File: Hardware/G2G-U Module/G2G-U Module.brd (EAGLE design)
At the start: 13.1 x 12.8 mm, 4 parts, among them J1 GROVE-4P-2.0-3470130P1

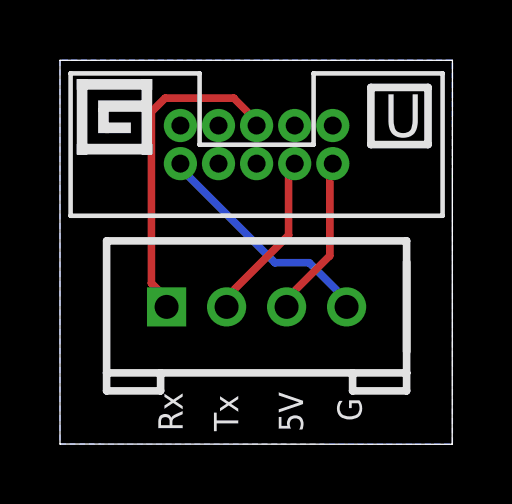
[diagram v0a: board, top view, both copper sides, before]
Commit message: Rotated the G plug 180 degrees.
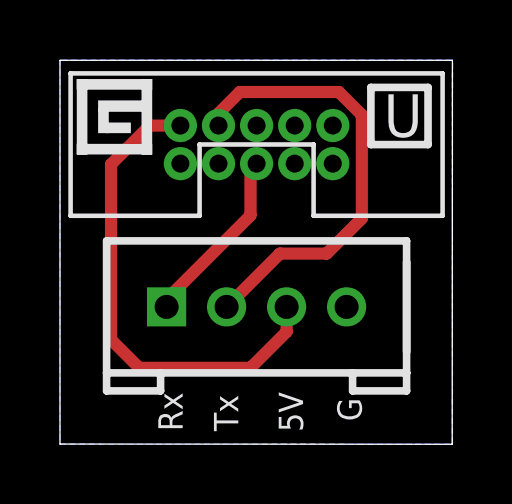
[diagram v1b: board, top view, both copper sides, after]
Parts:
- turned U$1 to 180 degrees
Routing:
- net +5V: track 5.39 -> 16.3 mm
- net TX: track 5.75 -> 15.0 mm
- net GND: track 7.74 -> 0.00 mm
- net RX: track 10.9 -> 6.02 mm
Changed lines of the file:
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@@
 <element name="J1" library="SoftDust" package="4P-2.0" value="GROVE-4P-2.0-3470130P1" x="6.5532" y="4.572" smashed="yes"/>
 <element name="LOGO1" library="SparkFun-Aesthetics" package="OSHW-LOGO-S" value="OSHW-LOGOS" x="1.8796" y="1.778" rot="MR0"/>
-<element name="U$1" library="SoftDust" package="2X5_1.27MM_FEMALE_PLUG" value="2X5_1.27MM_FEMALE_PLUG" x="6.5532" y="9.9822" rot="MR0"/>
+<element name="U$1" library="SoftDust" package="2X5_1.27MM_FEMALE_PLUG" value="2X5_1.27MM_FEMALE_PLUG" x="6.5532" y="9.9822" rot="MR180"/>
 <element name="FRAME1" library="SparkFun-Aesthetics" package="DUMMY" value="" x="0" y="-1.27">
 <attribute name="VERSION" value="v1.0" x="0" y="-1.27" size="1.778" layer="27" display="off"/>
@@
 <contactref element="U$1" pad="4"/>
 <contactref element="J1" pad="2"/>
-<wire x1="7.62" y1="6.9596" x2="7.62" y2="9.2456" width="0.254" layer="1"/>
-<wire x1="5.5626" y1="4.9022" x2="7.62" y2="6.9596" width="0.254" layer="1"/>
-<wire x1="7.62" y1="9.2456" x2="7.8232" y2="9.3472" width="0.254" layer="1"/>
-<wire x1="5.5626" y1="4.9022" x2="5.5532" y2="4.572" width="0.254" layer="1"/>
+<wire x1="5.5532" y1="4.572" x2="7.3312" y2="6.35" width="0.4064" layer="1"/>
+<wire x1="7.3312" y1="6.35" x2="8.89" y2="6.35" width="0.4064" layer="1"/>
+<wire x1="8.89" y1="6.35" x2="10.0584" y2="7.5184" width="0.4064" layer="1"/>
+<wire x1="10.0584" y1="7.5184" x2="10.0584" y2="10.9728" width="0.4064" layer="1"/>
+<wire x1="10.0584" y1="10.9728" x2="9.2964" y2="11.7348" width="0.4064" layer="1"/>
+<wire x1="9.2964" y1="11.7348" x2="5.9944" y2="11.7348" width="0.4064" layer="1"/>
+<wire x1="5.9944" y1="11.7348" x2="5.2832" y2="11.0236" width="0.4064" layer="1"/>
+<wire x1="5.2832" y1="11.0236" x2="5.2832" y2="10.6172" width="0.4064" layer="1"/>
 </signal>
 <signal name="RX">
 <contactref element="U$1" pad="5"/>
 <contactref element="J1" pad="1"/>
-<wire x1="6.477" y1="10.8458" x2="6.477" y2="10.6172" width="0.254" layer="1"/>
-<wire x1="5.7912" y1="11.5316" x2="6.477" y2="10.8458" width="0.254" layer="1"/>
-<wire x1="3.5052" y1="11.5316" x2="5.7912" y2="11.5316" width="0.254" layer="1"/>
-<wire x1="3.048" y1="11.0744" x2="3.5052" y2="11.5316" width="0.254" layer="1"/>
-<wire x1="3.048" y1="5.3594" x2="3.048" y2="11.0744" width="0.254" layer="1"/>
-<wire x1="3.5052" y1="4.9022" x2="3.048" y2="5.3594" width="0.254" layer="1"/>
-<wire x1="6.477" y1="10.6172" x2="6.5532" y2="10.6172" width="0.254" layer="1"/>
-<wire x1="3.5052" y1="4.9022" x2="3.5532" y2="4.572" width="0.254" layer="1"/>
+<wire x1="3.5532" y1="4.572" x2="3.5532" y2="4.8232" width="0.4064" layer="1"/>
+<wire x1="3.5532" y1="4.8232" x2="6.35" y2="7.62" width="0.4064" layer="1"/>
+<wire x1="6.35" y1="7.62" x2="6.35" y2="9.144" width="0.4064" layer="1"/>
+<wire x1="6.35" y1="9.144" x2="6.5532" y2="9.3472" width="0.4064" layer="1"/>
 </signal>
 <signal name="GND">
 <contactref element="U$1" pad="10"/>
 <contactref element="J1" pad="4"/>
-<wire x1="4.191" y1="9.017" x2="4.191" y2="9.2456" width="0.254" layer="16"/>
-<wire x1="7.1628" y1="6.0452" x2="4.191" y2="9.017" width="0.254" layer="16"/>
-<wire x1="8.3058" y1="6.0452" x2="7.1628" y2="6.0452" width="0.254" layer="16"/>
-<wire x1="9.4488" y1="4.9022" x2="8.3058" y2="6.0452" width="0.254" layer="16"/>
-<wire x1="4.191" y1="9.2456" x2="4.0132" y2="9.3472" width="0.254" layer="16"/>
-<wire x1="9.4488" y1="4.9022" x2="9.5532" y2="4.572" width="0.254" layer="16"/>
 <polygon width="0.254" layer="16" isolate="0.4064">
 <vertex x="0" y="0"/>
@@
 <contactref element="J1" pad="3"/>
 <contactref element="U$1" pad="2"/>
-<wire x1="8.9916" y1="6.2738" x2="8.9916" y2="9.2456" width="0.254" layer="1"/>
-<wire x1="7.62" y1="4.9022" x2="8.9916" y2="6.2738" width="0.254" layer="1"/>
-<wire x1="8.9916" y1="9.2456" x2="9.0932" y2="9.3472" width="0.254" layer="1"/>
-<wire x1="7.62" y1="4.9022" x2="7.5532" y2="4.572" width="0.254" layer="1"/>
+<wire x1="7.5532" y1="4.572" x2="7.5532" y2="3.7432" width="0.4064" layer="1"/>
+<wire x1="7.5532" y1="3.7432" x2="6.35" y2="2.54" width="0.4064" layer="1"/>
+<wire x1="6.35" y1="2.54" x2="2.6416" y2="2.54" width="0.4064" layer="1"/>
+<wire x1="2.6416" y1="2.54" x2="1.7018" y2="3.4798" width="0.4064" layer="1"/>
+<wire x1="1.7018" y1="3.4798" x2="1.7018" y2="9.3218" width="0.4064" layer="1"/>
+<wire x1="1.7018" y1="9.3218" x2="2.9972" y2="10.6172" width="0.4064" layer="1"/>
+<wire x1="2.9972" y1="10.6172" x2="4.0132" y2="10.6172" width="0.4064" layer="1"/>
 </signal>
 </signals>

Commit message: Replaced all 'G' logos with a new part for the logo.
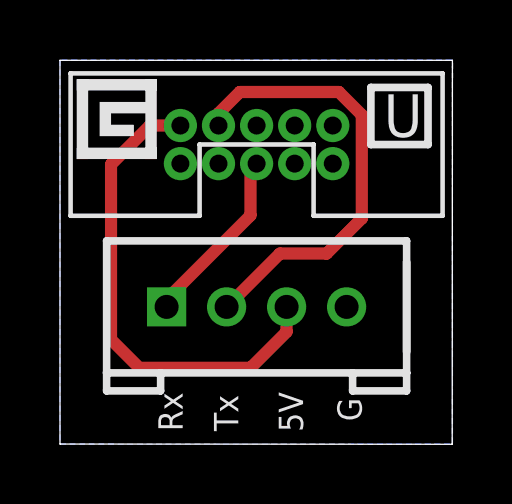
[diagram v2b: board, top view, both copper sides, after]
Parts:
- added U$2: GADGETEER_LOGO_SMALL, SoftDust:GADGETEER_LOGO_SMALL
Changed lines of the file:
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@@
 <text x="10.0584" y="0.762" size="0.8128" layer="21" font="vector" rot="R90">G</text>
 <text x="11.6332" y="6.0452" size="1.016" layer="22" font="vector" rot="MR0">Gadgeteer.in'</text>
-<rectangle x1="0.5588" y1="9.652" x2="3.0734" y2="10.0076" layer="21"/>
-<rectangle x1="0.5588" y1="11.811" x2="3.0734" y2="12.1666" layer="21"/>
-<rectangle x1="1.6383" y1="10.7315" x2="4.1529" y2="11.0871" layer="21" rot="R90"/>
-<rectangle x1="-0.5207" y1="10.7315" x2="1.9939" y2="11.0871" layer="21" rot="R90"/>
-<rectangle x1="1.27" y1="11.0744" x2="2.7432" y2="11.4554" layer="21"/>
-<rectangle x1="1.27" y1="10.3632" x2="1.6256" y2="11.2014" layer="21"/>
-<rectangle x1="1.7653" y1="10.1219" x2="2.1209" y2="10.9601" layer="21" rot="R90"/>
 </plain>
 <attributes>
@@
 <attribute name="DESIGNER" value="Ian Lee" x="0" y="-1.27" size="1.778" layer="27" display="off"/>
 </element>
+<element name="U$2" library="SoftDust" package="GADGETEER_LOGO_SMALL" value="GADGETEER_LOGO_SMALL" x="0.5588" y="9.4996"/>
 </elements>
 <signals>
